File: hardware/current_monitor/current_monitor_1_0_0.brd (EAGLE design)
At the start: 25.1 x 79.6 mm, 61 parts, among them Q1 RZQ045P01CT, Q2 APDS-9002, U1 PIC18F46J50, U4 MAX4372, U5 TC1046, U6 AT45DB041BWIDE, U7 AT45DB041BWIDE, X1 USBSMD

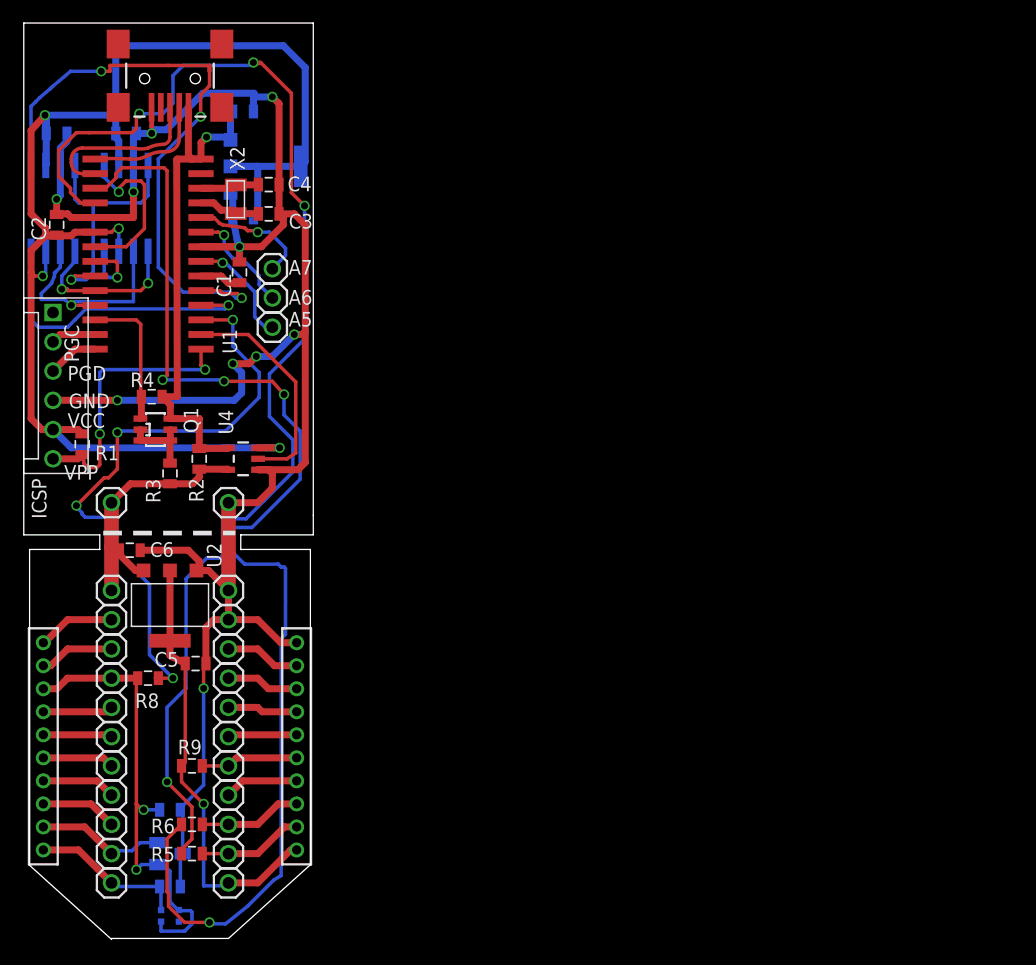
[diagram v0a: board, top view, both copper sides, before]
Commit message: current monitoring board changes
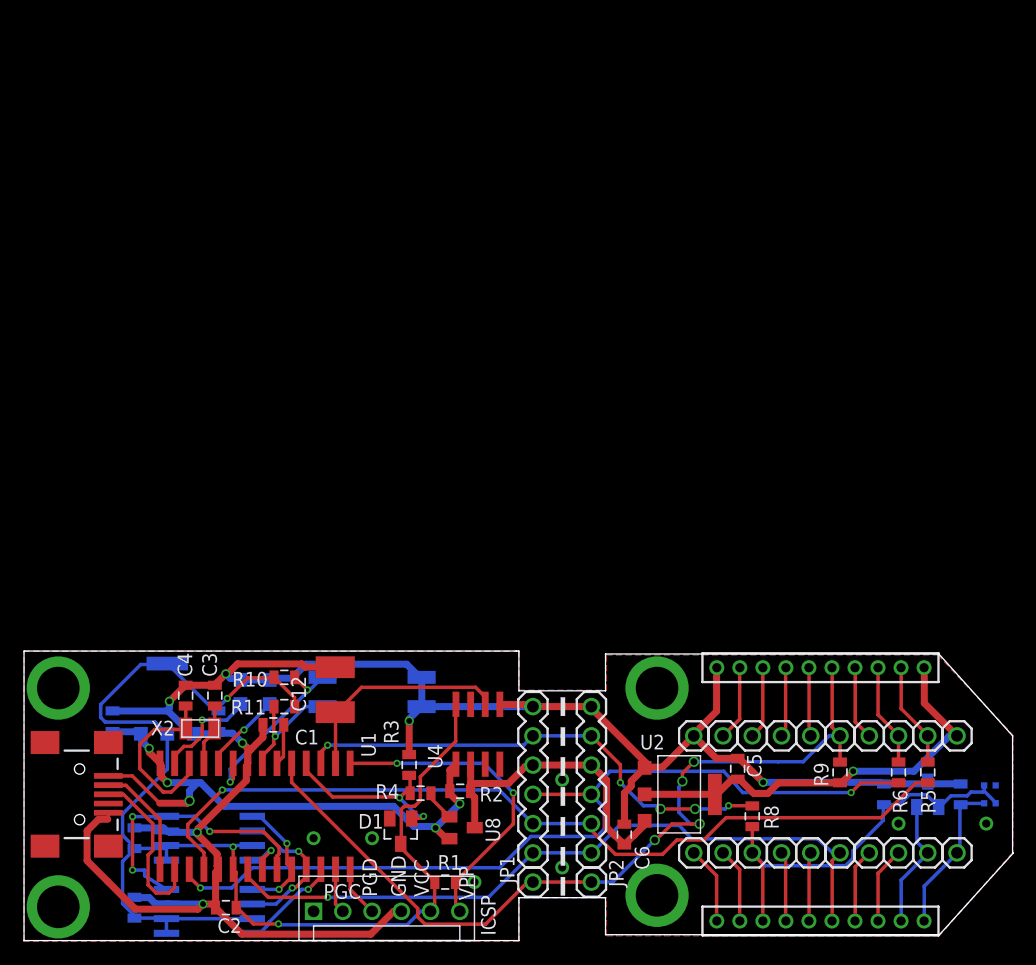
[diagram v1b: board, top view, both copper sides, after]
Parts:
- removed Q1: RZQ045P01CT, WSNlib:SOT23-6
- removed TP21, TP22, TP26, TP27: TESTPOINT100MIL, WSNlib:TESTPOINT-100MIL
- added C12: 10nF 1%, rcl:C1812
- added D1: BAS70, diode:SOT23
- added JP1, JP2: (no value), custom:1X06
- added LED1, LED2: (no value), led:CHIP-LED0805
- added R10, R11: 10k, SparkFun:0805
- added S1: 219-02, switch-dil:CTS-219-02
- added TP28, TP29: TESTPOINT100MIL, WSNlib:TESTPOINT-100MIL
- added TP30, TP31, TP32, TP33: TESTPOINTSMALLEST, WSNlib:TESTPOINT
- added TP34, TP35, TP36, TP37: TESTPOINTM3, WSNlib:M3_HOLE
- added U8: ZXCT1009, WSNlib:SOT23
- R2: value 1.2K -> 2.2 1%
- R3: value 75m -> 470 1%
- R4: value 1K -> 200
- TP20, TP24, TP25: value TESTPOINT100MIL -> TESTPOINTSMALLEST; device WSNlib:TESTPOINT-100MIL -> WSNlib:TESTPOINT
- U4: value MAX4372 -> MAX4172; device WSNlib:SOT23-5 -> WSNlib:SO08
- moved TP20 75.5 mm to (83.6, 10.2)
- moved TP10 73.5 mm to (81.0, 7.69), turned to 90 degrees
- moved Q2 72.0 mm to (83.9, 12.8), turned to 180 degrees
- moved TP11 70.9 mm to (78.5, 7.69), turned to 90 degrees
- moved R7 69.1 mm to (81.4, 12.8), turned to 270 degrees
- moved TP12 68.4 mm to (76.0, 7.69), turned to 90 degrees
- moved C9 67.6 mm to (9.61, 2.93), turned to 270 degrees
- moved U5 66.0 mm to (78.5, 12.8), turned to 0 degrees
- moved TP13 66.0 mm to (73.4, 7.69), turned to 90 degrees
- moved TP1 64.5 mm to (81.0, 17.9), turned to 90 degrees
- moved R5 64.3 mm to (78.5, 14.7), turned to 90 degrees
- moved TP14 63.7 mm to (70.9, 7.69), turned to 90 degrees
- moved X1 62.7 mm to (4.85, 12.8), turned to 0 degrees
- moved U7 62.4 mm to (16.3, 2.61), turned to 270 degrees
- moved C11 62.0 mm to (74.7, 12.8), turned to 90 degrees
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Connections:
- removed net AT1_WP: U1.21, U6.5
- removed net AT2_WP: U1.5, U7.5
- removed net HIGH_CURRENT: Q1.3, R4.1, U1.26
- removed net N$14: R6.1, U1.17
- removed net N$20: R9.1, TP23.2, U$2.5
- removed net N$29: TP14.2, U$2.16
- new net MOTE_RESET: R9.1, TP23.2, TP28.2, TP29.2, U$2.5, U1.5
- new net MOTE_RTS: JP1.6, JP2.6, TP14.2, U$2.16, U1.21
- new net RES_M2P: JP1.5, JP2.5, R5.1, U1.18
- new net RES_P2M: JP1.4, JP2.4, R6.1, U1.17
- new net VCC_MOTE: C6.1, JP1.3, JP2.3, R2.1, U2.3, U4.2, U8.3
- net AT2_CS: now also U1.26; no longer U1.4
- net EXTRA1: now also R11.1, S1.3; no longer TP20.2
- net EXTRA2: now also R10.1, S1.4; no longer TP21.2
- net EXTRA3: now also LED2.A; no longer TP22.2
- net GND: now also C12.2, JP1.1, JP2.1, LED1.C, LED2.C, R3.2, S1.1, S1.2, TP20.P$1, TP24.P$1, TP25.P$1, TP30.P$1, TP31.P$1, TP32.P$1, TP33.P$1, TP34.P$1, TP35.P$1, TP36.P$1, TP37.P$1, U4.5; no longer TP25.2, TP27.2, U4.1
- net MOTE_ASSOC: now also JP1.2, JP2.2
- net N$11: now also C12.1, U4.6; no longer U4.2
- net N$12: now also D1.1, R3.1, R4.2, U1.4; no longer Q1.1, Q1.2, Q1.5, Q1.6, R3.2
- net N$13: now also R4.1, U8.1; no longer R5.1, U1.18
- net N$3: now also LED1.A, U1.13; no longer C6.1, R2.1, R3.1, TP24.2, TP26.2, U2.3, U4.5
- net VCC: now also D1.3, R10.2, R11.2, U4.8, U6.5, U7.5; no longer U4.3
- net VUSB: now also U4.1, U8.2; no longer Q1.4, R4.2, U4.4
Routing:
- net N$13: track 110.0 -> 2.71 mm, vias 4 -> 0
- net N$14: track 106.3 -> 0.00 mm, vias 4 -> 0
- net RES_P2M: track 0.00 -> 76.6 mm, vias 0 -> 2
- net MOTE_RESET: track 0.00 -> 75.4 mm, vias 0 -> 4
- net RES_M2P: track 0.00 -> 75.2 mm, vias 0 -> 1
- net MOTE_RTS: track 0.00 -> 62.6 mm, vias 0 -> 1
- net AT2_WP: track 54.8 -> 0.00 mm, vias 3 -> 0
- net VCC_MOTE: track 0.00 -> 27.7 mm
- net AT2_CS: track 26.5 -> 8.73 mm
- net N$3: track 23.8 -> 9.13 mm, vias 0 -> 1
- net AT1_WP: track 14.5 -> 0.00 mm, vias 1 -> 0
- net HIGH_CURRENT: track 13.0 -> 0.00 mm
- net MOTE_ASSOC: track 53.7 -> 42.7 mm, vias 4 -> 5
- net VCC: track 128.8 -> 117.9 mm, vias 4 -> 3
- net N$6: track 5.11 -> 15.4 mm
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- added copper zone on layer 1, net GND
- added copper zone on layer 16, net GND
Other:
- board size 25.1 x 79.6 mm -> 85.9 x 25.1 mm
- board text added: "5V"
- board text added: "AWAKE"
- board text added: "OFF"
- board text added: "ON"
- board text added: "RST"
- board text added: "RTS"
- board text added: "RX"
- board text added: "SW1"
- board text added: "SW2"
- board text added: "TX"
- board text removed: "A5"
- board text removed: "A6"
- board text removed: "A7"
